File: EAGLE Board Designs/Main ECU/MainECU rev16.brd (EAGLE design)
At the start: 97.5 x 115.6 mm, 363 parts, among them J1 CONNECTOR-24_CONNECTOR-24_, J2 CONNECTOR-24_CONNECTOR-24_, K1 RELAY_DPDT_07DSMT, K2 RELAY_DPDT_07DSMT, K3 RELAY_DPDT_07DSMT, K4 RELAY_DPDT_07DSMT, K5 RELAY_DPDT_07DSMT, Q1 TRANSISTOR_N_MOS__DMG3406L-7, Q2 TRANSISTOR_P_MOS_SOT-23_DMP30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, Q3 TRANSISTOR_P_MOS_SOT-23_DMP30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, Q4 TRANSISTOR_N_MOS__DMG3406L-7, U1 VOLTAGE_REGULATOR_SOT-223_3.3V, U10 LOGICGATE_OR, U11 LOGICGATE_OR, U12 LOGICGATE_OR, U13 LOGICGATE_NOR, U14 TCAN1051HQV-Q1, U15 LOGICGATE_AND_DCK3, U16 MAX3074EESA+, U17 MAX7400, U18 MAX7400, U19 OPAMP_2_CHANNEL_OPA_2991, U2 MCP3208, U20 OPAMP_2_CHANNEL_OPA_2991, U21 OPAMP_2_CHANNEL_OPA_2991, U22 OPAMP_2_CHANNEL_OPA_2991, U23 OPAMP_2_CHANNEL_OPA_2991, U24 OPAMP_2_CHANNEL_OPA_2991, U25 OPAMP_2_CHANNEL_OPA_2991, U26 OPAMP_2_CHANNEL_OPA_2991, U27 OPAMP_2_CHANNEL_OPA_2991, U28 OPAMP_1_CHANNEL_OPA991, U29 TCAN1051HQV-Q1, U3 OPAMP_1_CHANNEL_OPA991, U30 TCAN1051HQV-Q1, U31 ADM8316WBX30, U32 OPAMP_2_CHANNEL_OPA_2991, U33 OPAMP_1_CHANNEL_OPA991, U34 OPAMP_1_CHANNEL_OPA991, U35 OPAMP_1_CHANNEL_OPA991, U4 TCAN1051HQV-Q1, U5 OPAMP_1_CHANNEL_OPA991, U6 MCP3208, U7 OPAMP_1_CHANNEL_OPA991, U8 LOGICGATE_OR, U9 LOGICGATE_OR

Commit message: rev16 schematic done
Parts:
- removed D2: SCHOTTKY_1206_40V, HyTechDevices:1206-DIODE
- added D1: ZENER_1.5SMBJ_12V, HyTechDevices:1.5SMBJ
- added Q5: TRANSISTOR_P_MOS_SOT-23_DMP3056L-7, HyTechDevices:SOT-23
- added R127: RESISTOR_0603_100K, HyTechDevices:0603-RES
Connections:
- removed net !FL_CS: A2.D33
- removed net !FR_CS: A2.D29
- new net 24VIN: J1.22, Q5.3
- net !AD2_CS: now also A2.D33
- net +24V: now also D1.2, Q5.2; no longer D2.2
- net GND: now also R127.1
- net N$36: now also D1.1, Q5.1, R127.2; no longer D2.1, J1.22
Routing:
- net !FL_CS: track 33.5 -> 0.00 mm, vias 2 -> 0
- net !AD2_CS: track 0.00 -> 33.5 mm, vias 0 -> 2
- net !FR_CS: track 25.1 -> 0.00 mm, vias 2 -> 0
- net N$36: track 14.8 -> 0.00 mm
- net 24VIN: track 0.00 -> 11.7 mm

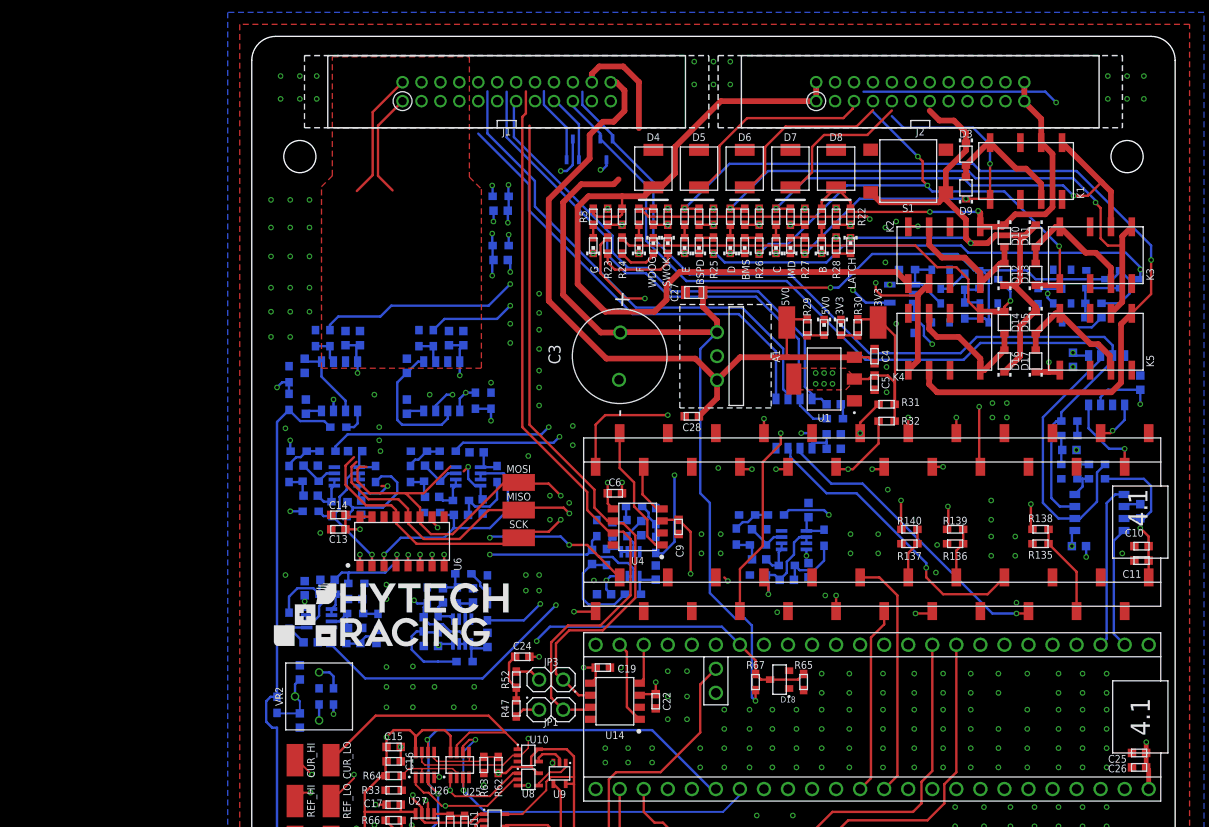
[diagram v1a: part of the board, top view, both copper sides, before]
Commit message: moving around diff pairs
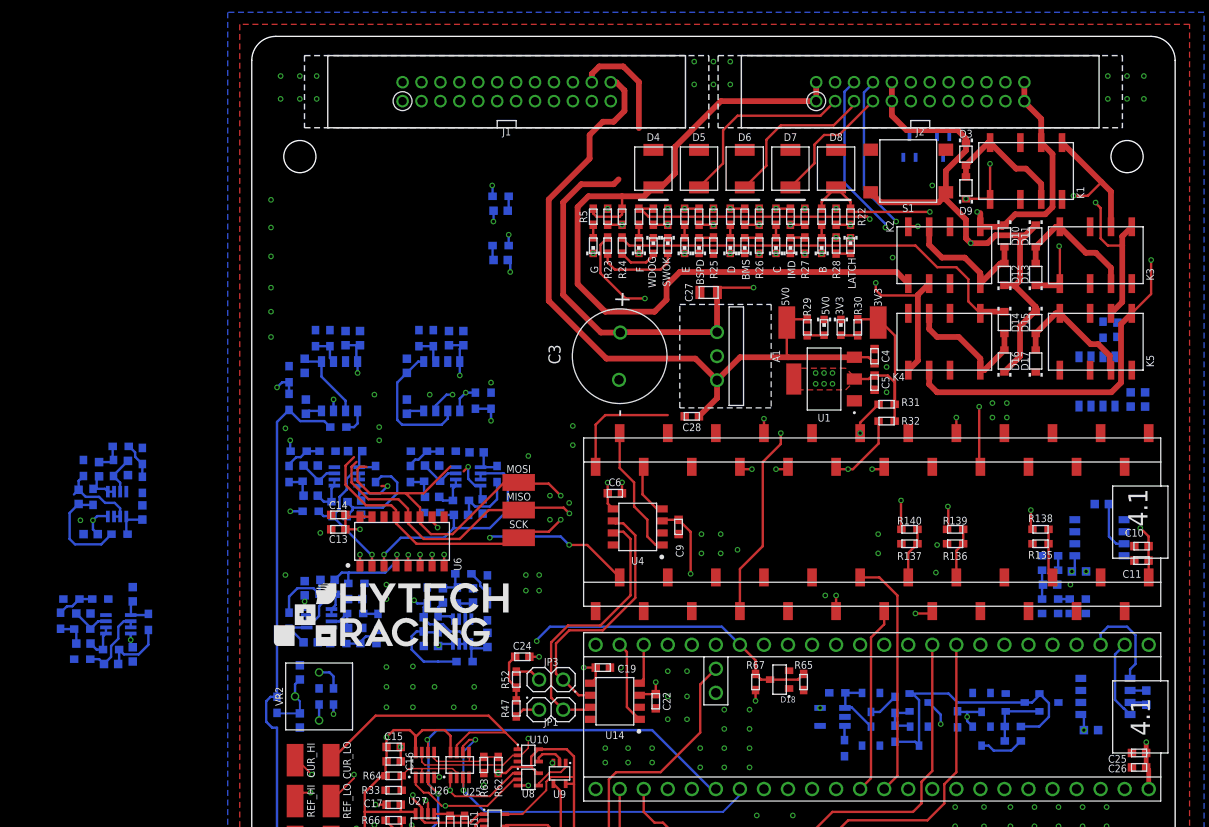
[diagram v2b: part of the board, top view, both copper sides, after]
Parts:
- moved C75 71.9 mm to (-12.6, 50.3)
- moved C76 71.9 mm to (-17.8, 54.6)
- moved C77 71.9 mm to (-12.6, 56.6)
- moved C78 71.9 mm to (-14.9, 49.3)
- moved C79 71.9 mm to (-17.8, 51.4)
- moved R111 71.9 mm to (-20.2, 53.8)
- moved R112 71.9 mm to (-14.9, 50.8)
- moved R113 71.9 mm to (-17.9, 53.0)
- moved R114 71.9 mm to (-10.9, 53.7)
- moved R115 71.9 mm to (-17.9, 49.8)
- moved R116 71.9 mm to (-16.0, 56.1)
- moved R117 71.9 mm to (-19.1, 56.1)
- moved U23 71.9 mm to (-14.1, 53.5)
- moved C69 54.6 mm to (-17.0, 63.0)
- moved C80 54.6 mm to (-13.1, 70.0)
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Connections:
- net INERTIA_SENSE: now also A2.D22; no longer A2.D23
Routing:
- net BRAKE_2_EXT: track 116.4 -> 0.00 mm, vias 1 -> 0
- net THERM_FR: track 117.5 -> 1.57 mm, vias 3 -> 0
- net THERM_FL: track 108.2 -> 1.57 mm, vias 3 -> 0
- net CANL_2: track 101.7 -> 0.00 mm
- net BRAKE_1_EXT: track 96.2 -> 0.00 mm, vias 1 -> 0
- net CANH_2: track 95.2 -> 0.00 mm
- net BSPD_OK_LV: track 113.9 -> 24.2 mm
- net ACCEL_2_EXT: track 88.1 -> 0.00 mm, vias 1 -> 0
- net STEERING_1_EXT: track 82.9 -> 0.00 mm, vias 1 -> 0
- net ACCEL_1_EXT: track 74.5 -> 0.00 mm, vias 1 -> 0
- net REFERENCE_EXT: track 72.2 -> 0.00 mm, vias 1 -> 0
- net SOFTWARE_OK: track 79.1 -> 11.4 mm, vias 5 -> 1
- net BSPD_OK: track 67.2 -> 0.00 mm, vias 3 -> 0
- net STEERING_2_EXT: track 63.7 -> 0.00 mm, vias 1 -> 0
- net CURRENT_EXT: track 60.0 -> 0.00 mm, vias 1 -> 0
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- removed copper zone on layer 1, net NO_FILL

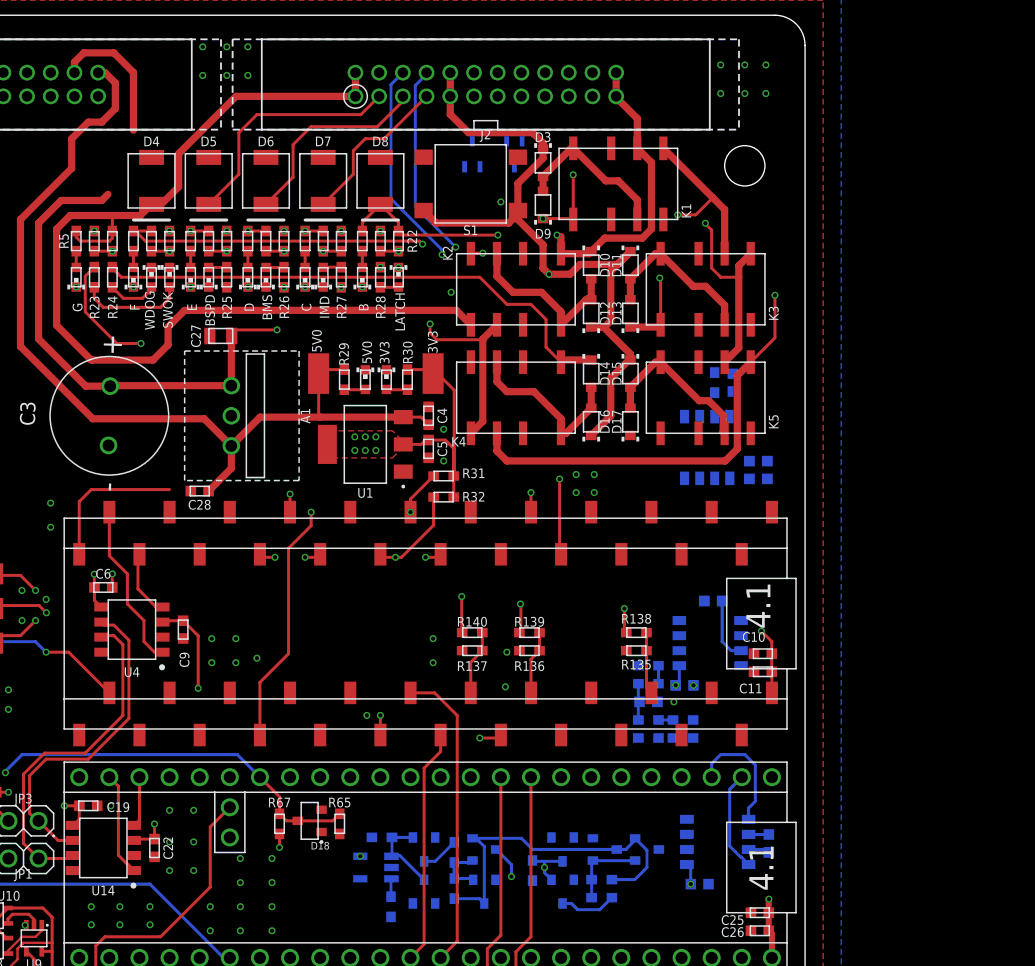
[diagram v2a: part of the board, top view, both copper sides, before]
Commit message: diff pairs routed
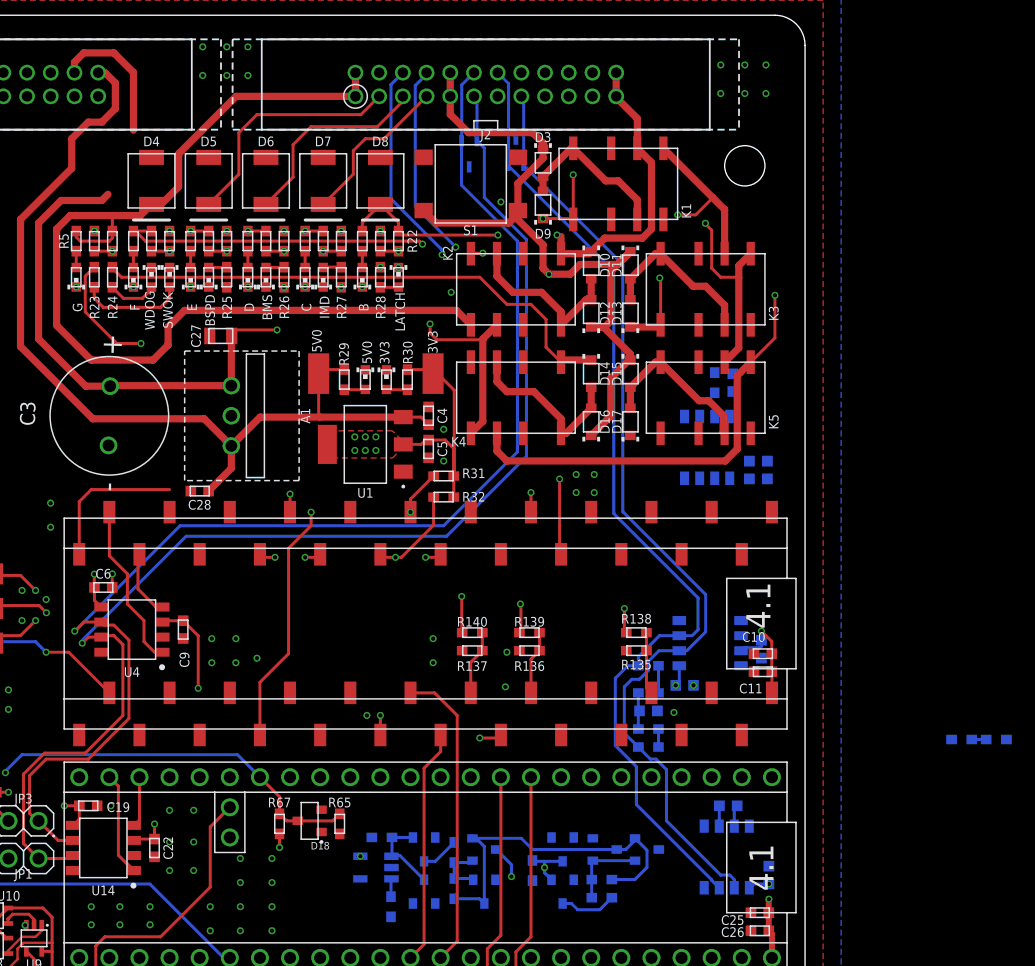
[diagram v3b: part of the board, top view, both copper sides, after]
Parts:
- moved JP12 26.4 mm to (113.7, 54.5)
- moved JP11 26.4 mm to (110.7, 54.5)
- moved C59 5.89 mm to (94.5, 43.1), turned to 90 degrees
- moved C62 5.75 mm to (93.9, 62.1), turned to 270 degrees
- moved C60 4.67 mm to (91.1, 48.9), turned to 0 degrees
- moved JP2 3.71 mm to (84.3, 53.8), turned to 180 degrees
- moved U29 1.48 mm to (90.9, 44.6), turned to 180 degrees
- moved C61 0.76 mm to (84.3, 56.9)
- moved R141 0.76 mm to (84.3, 55.4)
- moved R142 0.76 mm to (84.3, 58.4)
- moved D24 0.25 mm to (69.2, 103.9), turned to 270 degrees
- moved D23 0.18 mm to (73.2, 104.0), turned to 90 degrees
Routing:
- net CANH_2: track 0.00 -> 84.5 mm
- net CANL_2: track 0.00 -> 82.3 mm
- net CANL_3: track 27.7 -> 108.2 mm, vias 0 -> 1
- net CANH_3: track 29.2 -> 107.4 mm, vias 0 -> 1
- net CAN_TCU_TX2: track 10.3 -> 0.00 mm
- net CAN_TCU_RX2: track 8.47 -> 0.00 mm
- net +5V: track 518.0 -> 515.8 mm
- net N$11: track 0.00 -> 1.22 mm
- net N$2: track 1.52 -> 2.29 mm

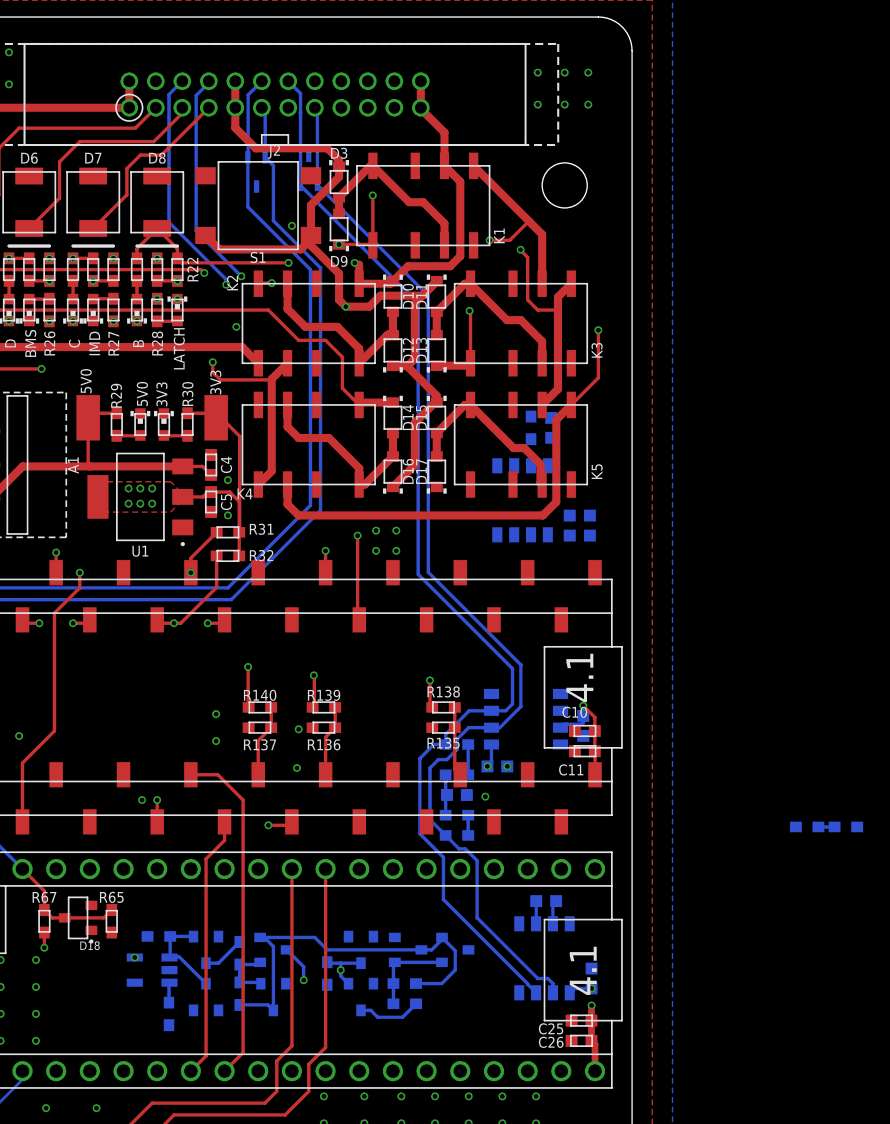
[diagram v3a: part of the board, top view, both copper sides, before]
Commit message: finished diff pairs
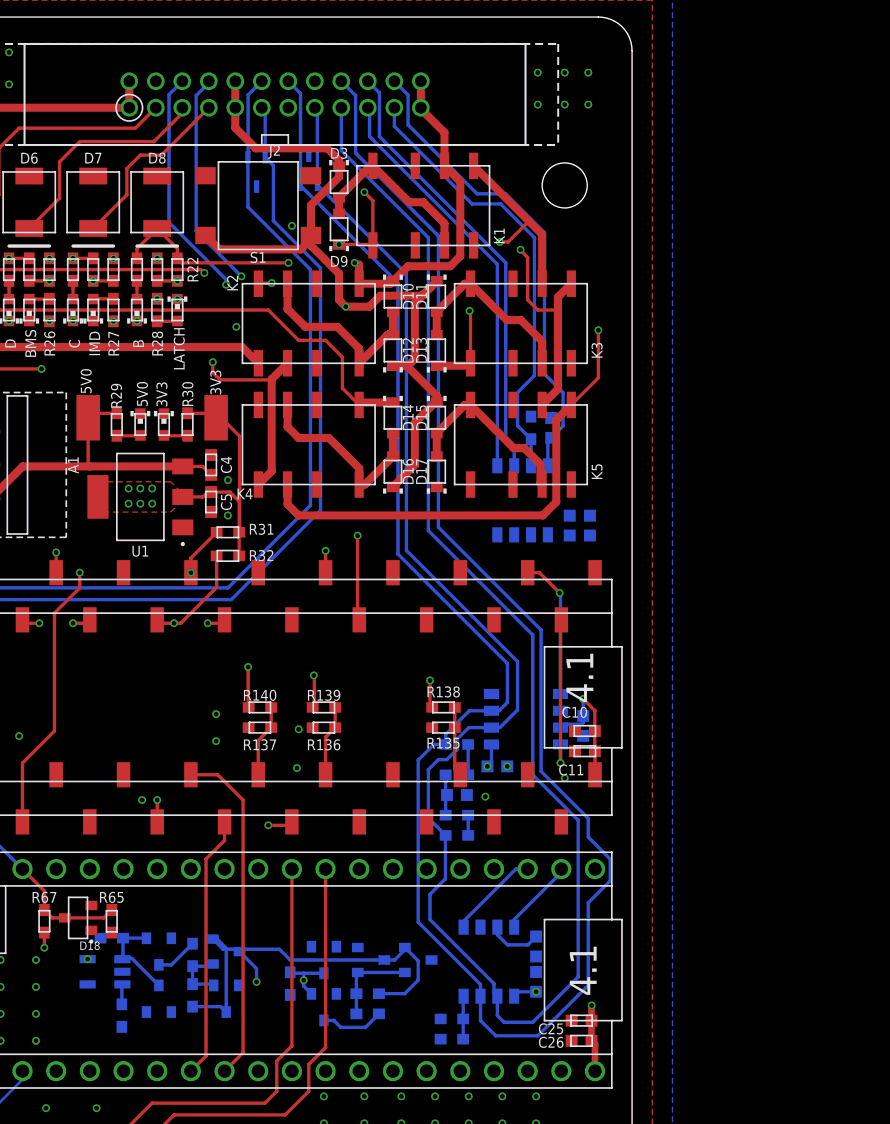
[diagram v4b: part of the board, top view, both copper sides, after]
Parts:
- moved JP12 33.8 mm to (83.9, 38.5), turned to 0 degrees
- moved JP11 30.5 mm to (83.9, 40.0)
- moved C59 4.20 mm to (90.3, 42.8)
- moved U29 4.20 mm to (86.7, 44.3)
- moved Q4 3.56 mm to (61.8, 45.1)
- moved U31 3.56 mm to (57.8, 43.6)
- moved D20 3.56 mm to (61.8, 41.5)
- moved Q3 3.56 mm to (66.9, 45.1)
- moved R143 3.56 mm to (59.1, 40.3)
- moved R149 3.56 mm to (58.3, 46.1)
- moved D19 3.56 mm to (66.9, 41.5)
- moved R145 3.56 mm to (64.4, 41.8)
- moved R148 3.56 mm to (64.4, 44.8)
- moved C60 3.51 mm to (90.3, 45.5), turned to 270 degrees
- moved R144 2.90 mm to (77.6, 40.4)
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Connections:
- net CANH_2: now also J2.18; no longer J2.17
- net CANL_2: now also J2.17; no longer J2.18
- net RS422_RX_N: now also J2.21; no longer J2.22
- net RS422_RX_P: now also J2.22; no longer J2.21
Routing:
- net CANH_2: track 84.5 -> 171.8 mm
- net CANL_2: track 82.3 -> 163.5 mm
- net RS422_RX_P: track 0.00 -> 36.0 mm
- net RS422_RX_N: track 0.00 -> 33.6 mm
- net RS422_TX_N: track 0.00 -> 33.6 mm
- net RS422_TX_P: track 0.00 -> 31.0 mm
- net CAN_ECU_RX2: track 0.00 -> 12.2 mm, vias 0 -> 1
- net CAN_ECU_TX2: track 0.00 -> 10.7 mm, vias 0 -> 1
- net CAN_TCU_TX2: track 0.00 -> 6.90 mm
- net CAN_TCU_RX2: track 0.00 -> 5.85 mm
- net +5V: track 515.8 -> 519.6 mm
- net N$11: track 1.22 -> 3.25 mm
- net GND: track 25.4 -> 23.7 mm, vias 244 -> 240
- net +24V: track 115.2 -> 116.2 mm

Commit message: work
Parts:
- added JP5, JP6, JP7, JP8: JUMPER__1X02, HyTechDevices:1X02
- added R128, R129, R130, R150: RESISTOR_0603_20K, HyTechDevices:0603-RES
- moved C1 78.4 mm to (13.0, 60.7), turned to 270 degrees
- moved C2 77.5 mm to (11.3, 60.7), turned to 270 degrees
- moved U2 76.2 mm to (8.38, 65.7), turned to 180 degrees
- moved C75 70.5 mm to (-64.1, 98.4), turned to 90 degrees
- moved C32 69.6 mm to (-34.2, 124.3)
- moved C33 69.6 mm to (-28.2, 131.6)
- moved C34 69.6 mm to (-29.7, 131.6)
- moved C37 69.6 mm to (-44.8, 124.3)
- moved C51 69.6 mm to (-39.1, 131.6)
- moved C52 69.6 mm to (-40.6, 131.6)
- moved C67 69.6 mm to (-34.2, 128.7)
- moved C68 69.6 mm to (-45.0, 128.7)
- moved JP4 69.6 mm to (-41.4, 122.2)
- moved R1 69.6 mm to (-31.4, 131.6)
- moved R2 69.6 mm to (-32.9, 131.6)
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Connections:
- new net N$103: JP5.2, R102.1
- new net N$104: JP8.2, R88.1
- new net N$105: JP7.2, R95.1
- new net N$106: JP6.2, R109.1
- net ACCEL_1_EXT: now also JP8.1; no longer R88.1
- net ACCEL_2_EXT: now also JP7.1; no longer R95.1
- net BRAKE_1_EXT: now also JP5.1; no longer R102.1
- net BRAKE_2_EXT: now also JP6.1; no longer R109.1
- net FL_CORNER: now also R130.2
- net FR_CORNER: now also R150.2
- net GND: now also R128.1, R129.1, R130.1, R150.1
- net SUS_POT_1: now also R129.2
- net SUS_POT_2: now also R128.2
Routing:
- net CURRENT: track 142.4 -> 106.5 mm, vias 7 -> 5
- net BRAKE_1: track 64.6 -> 31.1 mm, vias 5 -> 3
- net ECU_SDO: track 74.0 -> 42.9 mm
- net REFERENCE: track 122.0 -> 93.0 mm
- net REFERENCE_3V3: track 30.3 -> 2.07 mm, vias 2 -> 0
- net ECU_SDI: track 69.8 -> 43.1 mm
- net ECU_CLK: track 66.2 -> 39.9 mm
- net ACCEL_1: track 26.3 -> 0.00 mm, vias 1 -> 0
- net 24V_SENSE_ECU: track 58.5 -> 32.3 mm, vias 2 -> 1
- net CURRENT_3V3: track 22.7 -> 1.65 mm, vias 2 -> 0
- net +3V3: track 61.9 -> 41.5 mm, vias 24 -> 17
- net !AD1_CS: track 23.2 -> 5.52 mm, vias 3 -> 1
- net BRAKE_2: track 17.2 -> 0.14 mm, vias 1 -> 0
- net +5V: track 519.6 -> 503.2 mm
- net ACCEL_2: track 15.5 -> 0.00 mm, vias 1 -> 0
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
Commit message: very nice
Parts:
- moved R128 135.1 mm to (-8.38, -15.4), turned to 180 degrees
- moved R129 129.1 mm to (-24.3, -18.3), turned to 180 degrees
- moved R150 78.4 mm to (-63.6, -67.9)
- moved R130 78.4 mm to (-63.6, -65.2)
- moved R43 26.0 mm to (-14.6, -12.7)
- moved R42 21.3 mm to (-14.6, -14.2), turned to 180 degrees
- moved U3 18.2 mm to (-26.8, -16.1), turned to 270 degrees
- moved C30 16.6 mm to (-11.8, -11.2), turned to 180 degrees
- moved C53 15.9 mm to (-11.7, -15.4), turned to 180 degrees
- moved C23 15.6 mm to (-27.2, -14.1), turned to 180 degrees
- moved R38 14.7 mm to (-33.0, -16.9)
- moved R35 14.5 mm to (-33.0, -15.4)
- moved R40 13.0 mm to (-30.1, -15.4)
- moved R37 12.6 mm to (-17.5, -14.2)
- moved R36 11.3 mm to (-17.5, -12.7)
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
